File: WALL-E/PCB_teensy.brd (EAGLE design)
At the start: 92.8 x 115.8 mm, 44 parts, among them U4 R-78E5.0-0.5

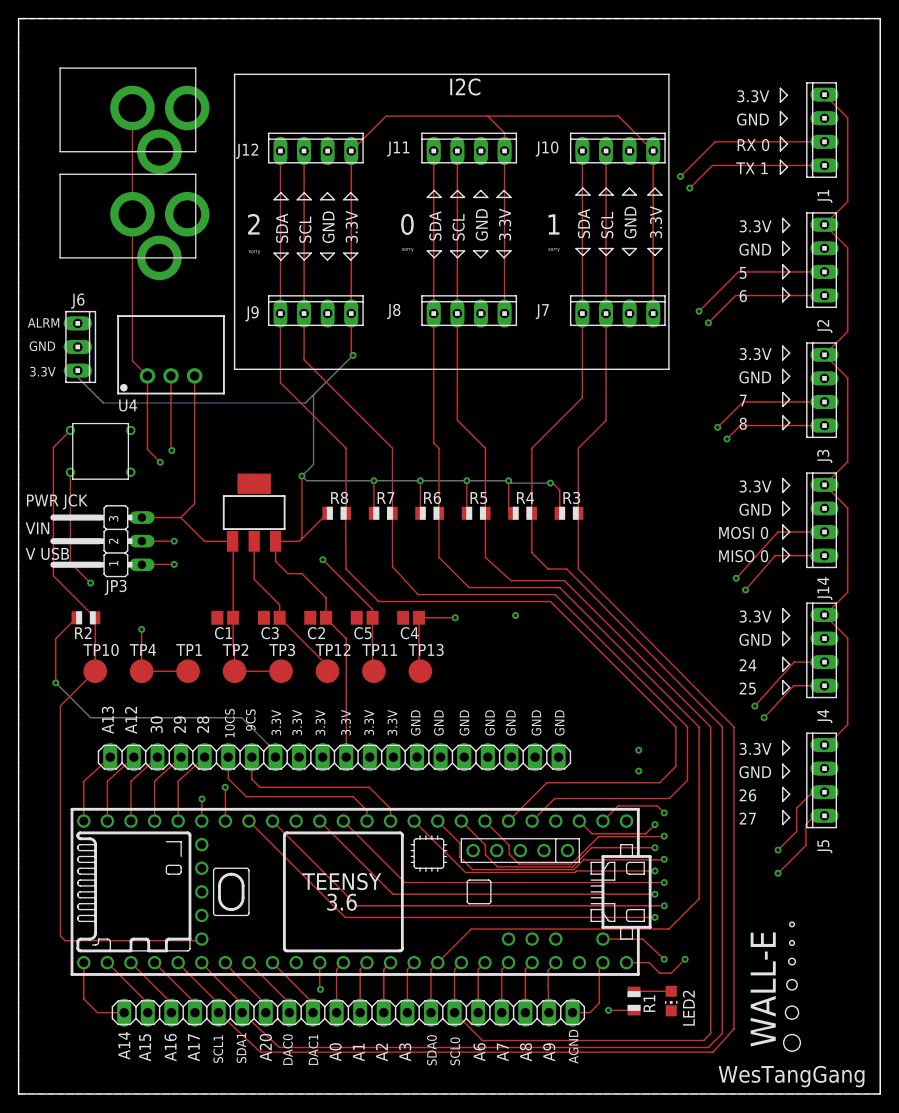
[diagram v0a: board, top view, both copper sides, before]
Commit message: removed extra top layer polygon and moved dimension to dimension layer. Also spaced out barrel jacks slightly
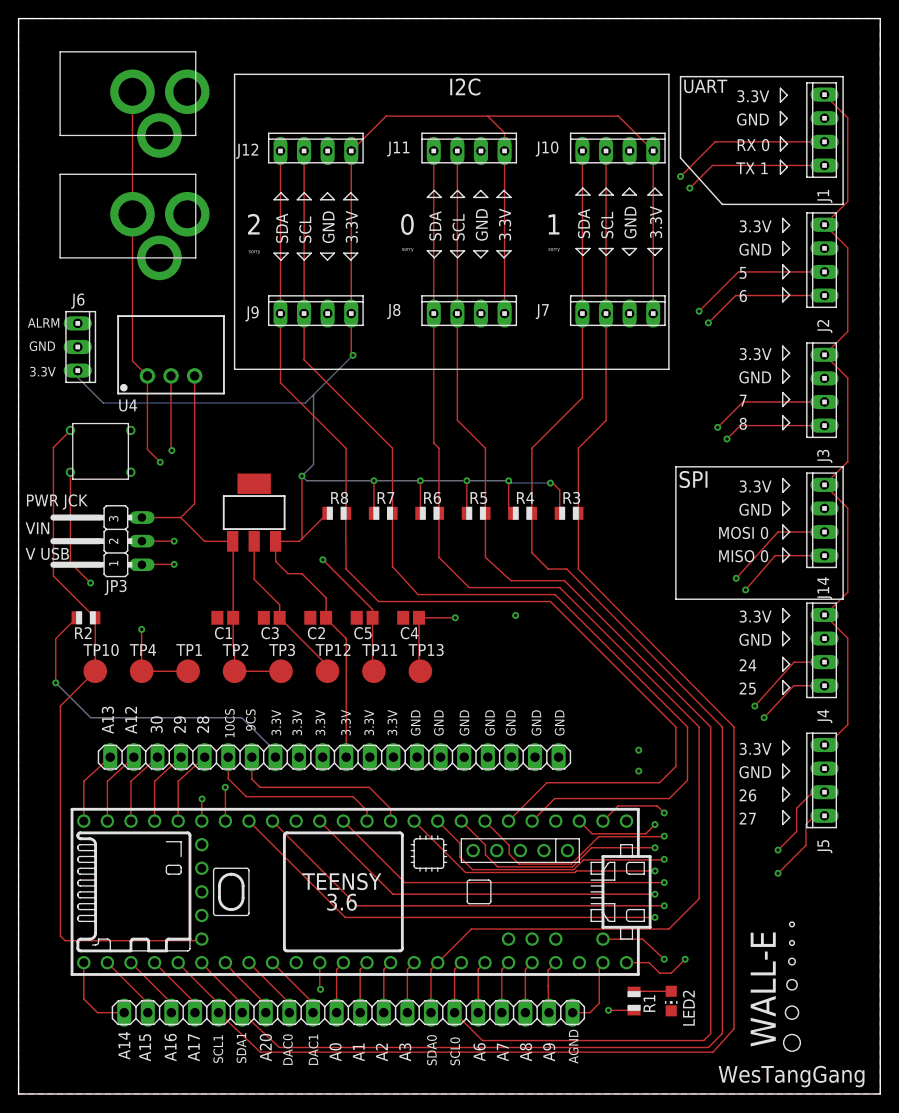
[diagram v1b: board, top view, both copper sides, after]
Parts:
- moved U$6 1.75 mm to (8.87, 107.8)
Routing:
- net +12V: track 67.7 -> 69.4 mm
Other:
- board text added: "SPI"
- board text added: "UART"

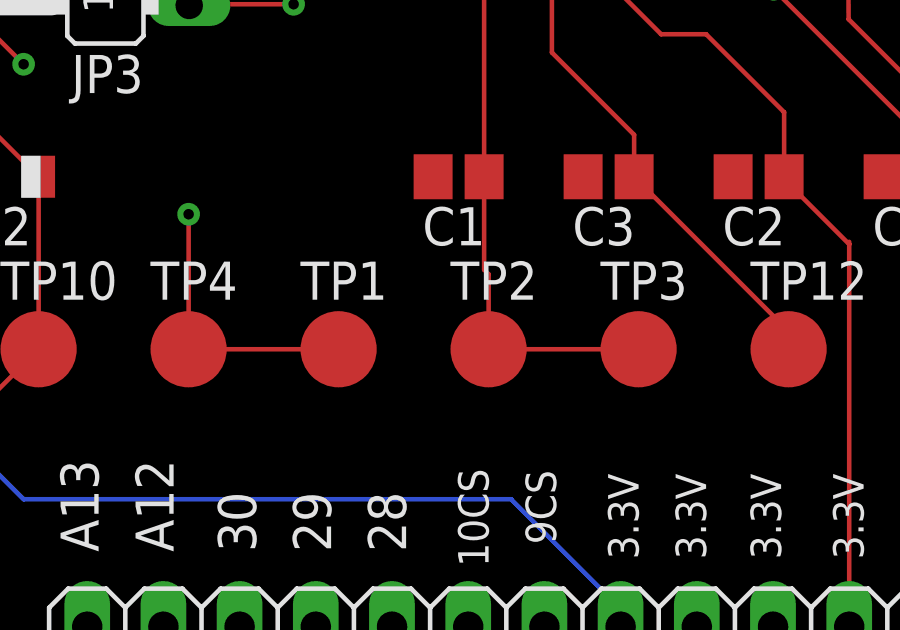
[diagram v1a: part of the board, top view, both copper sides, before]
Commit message: removed some test pins
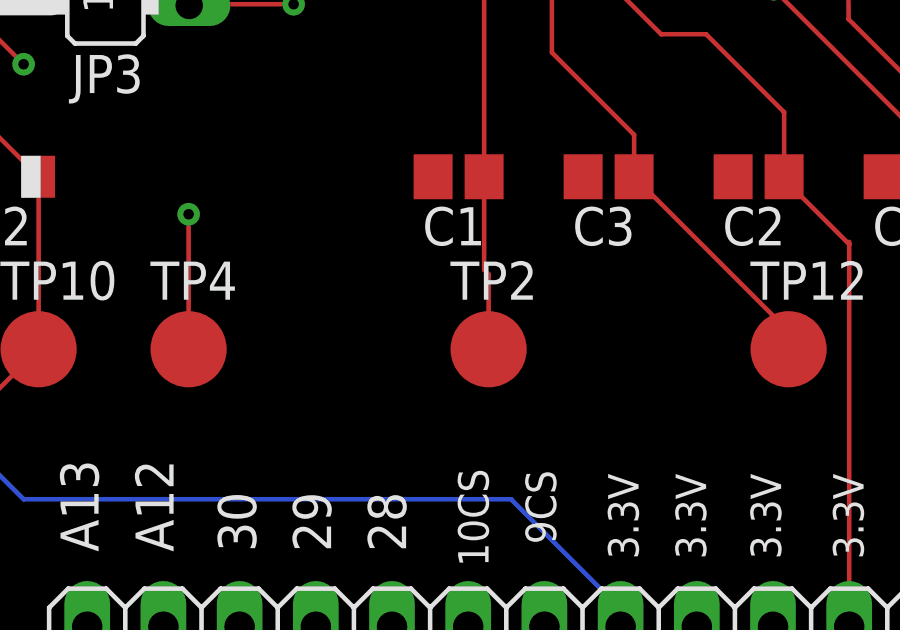
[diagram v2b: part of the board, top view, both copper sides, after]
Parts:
- removed TP1, TP3: PTR1B2,54, testpad:B2,54
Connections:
- net +12V: no longer TP1.TP
- net 5V: no longer TP3.TP
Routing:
- net 5V: track 45.9 -> 40.9 mm
- net +12V: track 69.4 -> 64.4 mm
- added copper zone on layer 15, net 3.3V
- removed copper zone on layer 2, net 3.3V

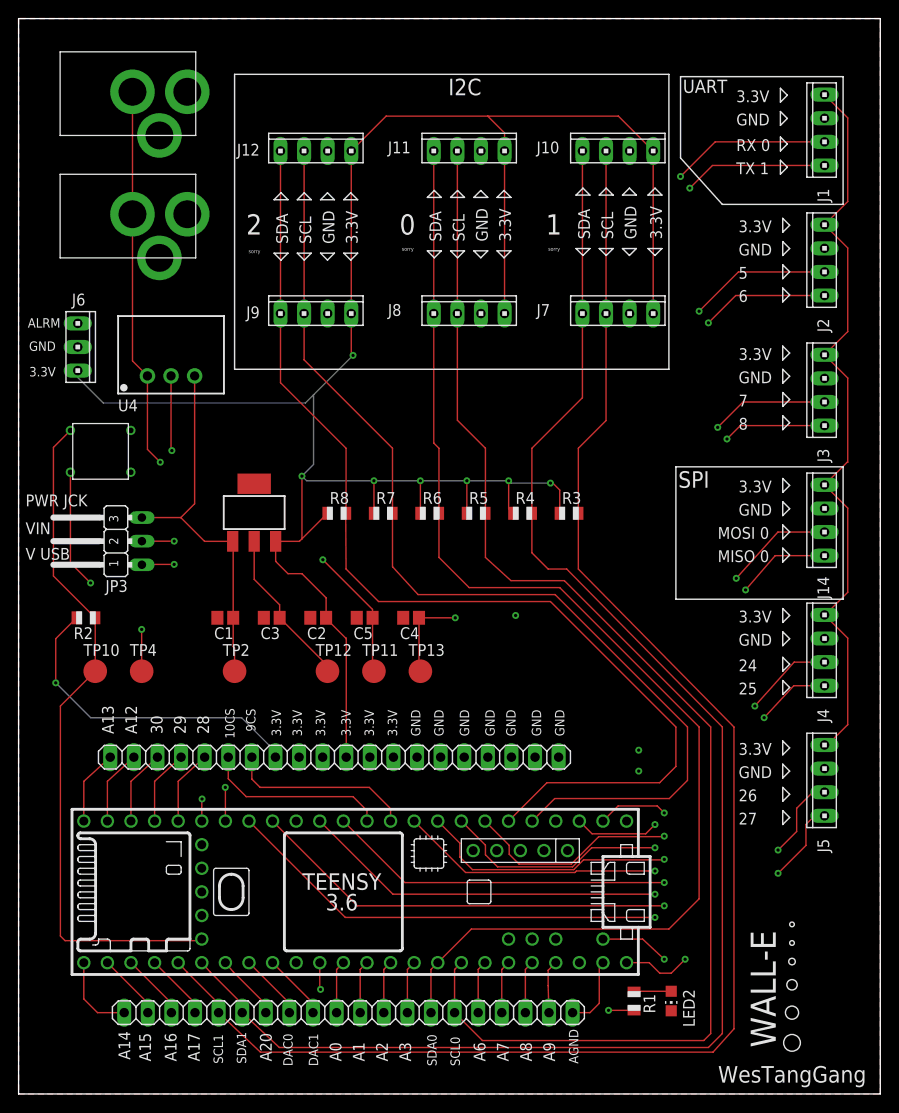
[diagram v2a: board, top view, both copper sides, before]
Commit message: removed 3.3v power routes, now components connect to the power plane
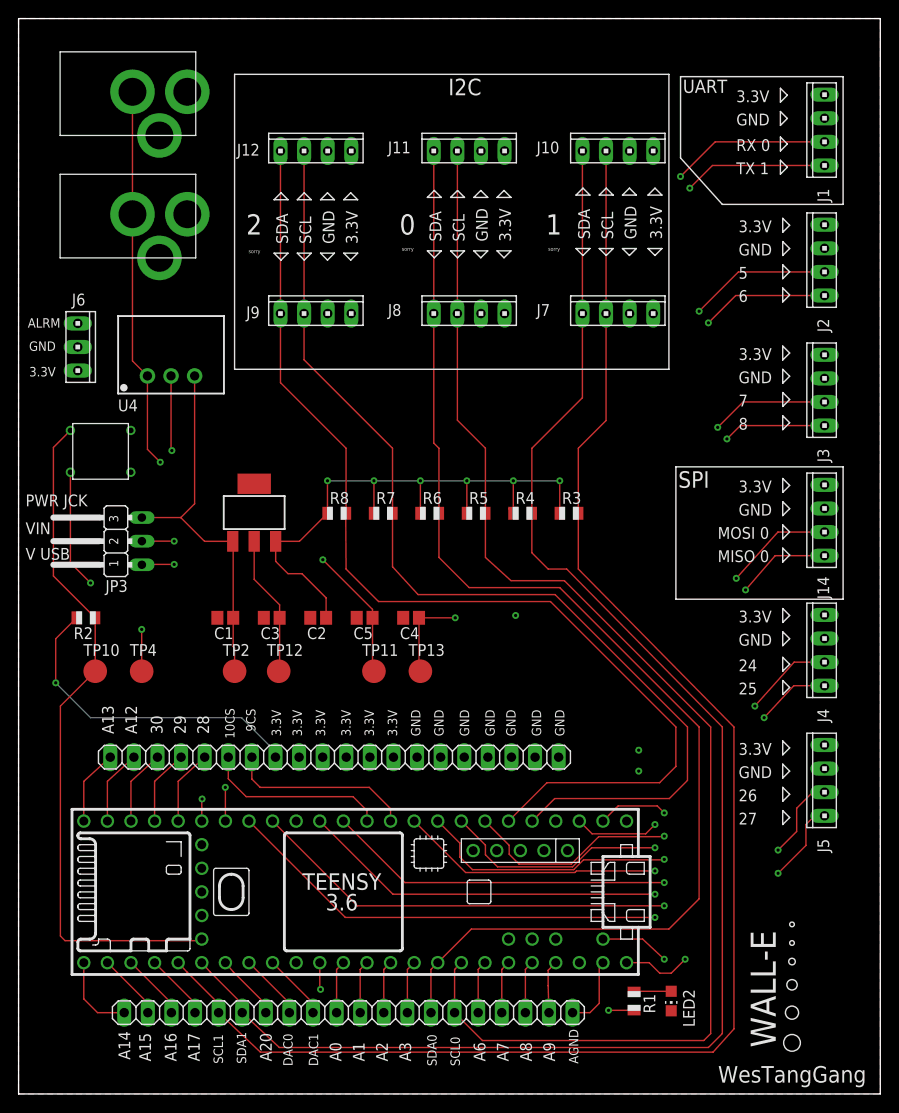
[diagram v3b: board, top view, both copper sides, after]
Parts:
- moved TP12 5.25 mm to (28.0, 45.5)
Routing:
- net 3.3V: track 342.3 -> 100.1 mm, vias 8 -> 7
- net ALARMPIN: track 95.5 -> 97.8 mm
- net N$3: track 17.2 -> 15.2 mm
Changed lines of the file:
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@@
 <attribute name="TP_SIGNAL_NAME" value="" x="38.25" y="45.5" size="1.778" layer="27" display="off"/>
 </element>
-<element name="TP12" library="testpad" library_urn="urn:adsk.eagle:library:385" package="B2,54" package3d_urn="urn:adsk.eagle:package:27948/1" value="PTR1B2,54" x="33.25" y="45.5">
-<attribute name="TP_SIGNAL_NAME" value="" x="33.25" y="45.5" size="1.778" layer="27" display="off"/>
+<element name="TP12" library="testpad" library_urn="urn:adsk.eagle:library:385" package="B2,54" package3d_urn="urn:adsk.eagle:package:27948/1" value="PTR1B2,54" x="28" y="45.5">
+<attribute name="TP_SIGNAL_NAME" value="" x="28" y="45.5" size="1.778" layer="27" display="off"/>
 </element>
 <element name="TP13" library="testpad" library_urn="urn:adsk.eagle:library:385" package="B2,54" package3d_urn="urn:adsk.eagle:package:27948/1" value="PTR1B2,54" x="43.25" y="45.5">
@@
 <wire x1="25.36" y1="55.39" x2="25.36" y2="59.4812" width="0.1524" layer="1"/>
 <wire x1="28.1" y1="52.65" x2="25.36" y2="55.39" width="0.1524" layer="1"/>
-<wire x1="28.1" y1="51.25" x2="33.25" y2="46.1" width="0.1524" layer="1"/>
-<wire x1="33.25" y1="46.1" x2="33.25" y2="45.5" width="0.1524" layer="1"/>
+<wire x1="28.1" y1="51.25" x2="28.1" y2="45.6" width="0.1524" layer="1"/>
+<wire x1="28.1" y1="45.6" x2="28" y2="45.5" width="0.1524" layer="1"/>
 </signal>
 <signal name="N$4">
@@
 <vertex x="0" y="115.75"/>
 </polygon>
-<wire x1="33.25" y1="62.5" x2="30.5" y2="59.75" width="0.1524" layer="1"/>
+<wire x1="33.25" y1="62.5" x2="30.2312" y2="59.4812" width="0.1524" layer="1"/>
 <wire x1="30.2312" y1="59.4812" x2="27.6714" y2="59.4812" width="0.1524" layer="1"/>
-<wire x1="35.81" y1="84" x2="35.81" y2="79.69" width="0.1524" layer="1"/>
-<wire x1="35.81" y1="79.69" x2="36" y2="79.5" width="0.1524" layer="1"/>
-<via x="36" y="79.5" extent="1-16" drill="0.35"/>
-<wire x1="36" y1="79.5" x2="31.75" y2="75.25" width="0.1524" layer="16"/>
-<via x="30.5" y="66.5" extent="1-16" drill="0.35"/>
-<wire x1="31.75" y1="75.25" x2="30.875" y2="74.375" width="0.1524" layer="16"/>
-<wire x1="30.5" y1="66.5" x2="30.5" y2="59.75" width="0.1524" layer="1"/>
-<wire x1="30.5" y1="59.75" x2="30.2312" y2="59.4812" width="0.1524" layer="1"/>
-<wire x1="6.37" y1="77.13" x2="6.37" y2="77.86" width="0.1524" layer="16"/>
-<wire x1="35.27" y1="49.08" x2="35.27" y2="49" width="0.1524" layer="1"/>
-<wire x1="35.27" y1="49" x2="35.27" y2="36.25" width="0.1524" layer="1"/>
-<wire x1="30.875" y1="74.375" x2="9.125" y2="74.375" width="0.1524" layer="16"/>
-<wire x1="9.125" y1="74.375" x2="6.37" y2="77.13" width="0.1524" layer="16"/>
-<wire x1="31.75" y1="75.25" x2="31.75" y2="67.75" width="0.1524" layer="16"/>
-<wire x1="31.75" y1="67.75" x2="30.5" y2="66.5" width="0.1524" layer="16"/>
+<via x="33.25" y="66" extent="1-16" drill="0.35"/>
 <wire x1="29" y1="56" x2="30.5" y2="56" width="0.1524" layer="1"/>
 <wire x1="29" y1="56" x2="27.6714" y2="57.3286" width="0.1524" layer="1"/>
 <wire x1="27.6714" y1="57.3286" x2="27.6714" y2="59.4812" width="0.1524" layer="1"/>
-<wire x1="35.81" y1="101.5" x2="35.81" y2="84" width="0.1524" layer="1"/>
-<wire x1="35.81" y1="101.5" x2="39.56" y2="105.25" width="0.1524" layer="1"/>
-<wire x1="39.56" y1="105.25" x2="50.5" y2="105.25" width="0.1524" layer="1"/>
-<wire x1="50.5" y1="105.25" x2="52.31" y2="103.44" width="0.1524" layer="1"/>
-<wire x1="52.31" y1="103.44" x2="52.31" y2="101.5" width="0.1524" layer="1"/>
-<wire x1="68.31" y1="101.5" x2="64.56" y2="105.25" width="0.1524" layer="1"/>
-<wire x1="64.56" y1="105.25" x2="50.5" y2="105.25" width="0.1524" layer="1"/>
-<wire x1="52.31" y1="101.5" x2="52.31" y2="84" width="0.1524" layer="1"/>
-<wire x1="86.75" y1="107.56" x2="89.25" y2="105.06" width="0.1524" layer="1"/>
-<wire x1="89.25" y1="96.06" x2="86.75" y2="93.56" width="0.1524" layer="1"/>
-<wire x1="89.25" y1="105.06" x2="89.25" y2="96.06" width="0.1524" layer="1"/>
-<wire x1="86.75" y1="93.56" x2="89.25" y2="91.06" width="0.1524" layer="1"/>
-<wire x1="89.25" y1="82.06" x2="86.75" y2="79.56" width="0.1524" layer="1"/>
-<wire x1="89.25" y1="91.06" x2="89.25" y2="82.06" width="0.1524" layer="1"/>
-<wire x1="86.75" y1="79.56" x2="89.25" y2="77.06" width="0.1524" layer="1"/>
-<wire x1="89.25" y1="77.06" x2="89.25" y2="68" width="0.1524" layer="1"/>
-<wire x1="89.25" y1="68" x2="89.19" y2="68" width="0.1524" layer="1"/>
-<wire x1="89.19" y1="68" x2="86.75" y2="65.56" width="0.1524" layer="1"/>
-<wire x1="86.75" y1="65.56" x2="89.25" y2="63.06" width="0.1524" layer="1"/>
-<wire x1="89.25" y1="63.06" x2="89.25" y2="54" width="0.1524" layer="1"/>
-<wire x1="89.25" y1="54" x2="86.81" y2="51.56" width="0.1524" layer="1"/>
-<wire x1="86.81" y1="51.56" x2="86.75" y2="51.56" width="0.1524" layer="1"/>
-<wire x1="86.75" y1="51.56" x2="89.25" y2="49.06" width="0.1524" layer="1"/>
-<wire x1="89.25" y1="49.06" x2="89.25" y2="39.75" width="0.1524" layer="1"/>
-<wire x1="89.25" y1="39.75" x2="87.06" y2="37.56" width="0.1524" layer="1"/>
-<wire x1="87.06" y1="37.56" x2="86.75" y2="37.56" width="0.1524" layer="1"/>
-<wire x1="68.31" y1="84" x2="68.31" y2="101.5" width="0.1524" layer="1"/>
-<wire x1="35.27" y1="49" x2="33.1" y2="51.17" width="0.1524" layer="1"/>
-<wire x1="33.1" y1="51.17" x2="33.1" y2="51.25" width="0.1524" layer="1"/>
 <wire x1="30.5" y1="56" x2="33.1" y2="53.4" width="0.1524" layer="1"/>
 <wire x1="33.1" y1="53.4" x2="33.1" y2="51.25" width="0.1524" layer="1"/>
-<wire x1="58.25" y1="62.5" x2="58.25" y2="65" width="0.1524" layer="1"/>
-<wire x1="58.25" y1="65" x2="57.25" y2="66" width="0.1524" layer="1"/>
-<wire x1="57.25" y1="66" x2="57.25" y2="65.75" width="0.1524" layer="1"/>
-<via x="57.25" y="65.75" extent="1-16" drill="0.35"/>
-<wire x1="57.25" y1="65.75" x2="53" y2="65.75" width="0.1524" layer="16"/>
-<wire x1="53" y1="65.75" x2="52.75" y2="66" width="0.1524" layer="16"/>
-<via x="52.75" y="66" extent="1-16" drill="0.35"/>
-<wire x1="52.75" y1="66" x2="52.75" y2="63" width="0.1524" layer="1"/>
+<via x="58.25" y="66" extent="1-16" drill="0.35"/>
+<via x="53.25" y="66" extent="1-16" drill="0.35"/>
 <wire x1="52.75" y1="63" x2="53.25" y2="62.5" width="0.1524" layer="1"/>
-<wire x1="52.75" y1="66" x2="48.25" y2="66" width="0.1524" layer="16"/>
+<wire x1="53.25" y1="66" x2="48.25" y2="66" width="0.1524" layer="16"/>
 <via x="48.25" y="66" extent="1-16" drill="0.35"/>
 <wire x1="48.25" y1="66" x2="48.25" y2="62.5" width="0.1524" layer="1"/>
@@
 <via x="38.25" y="66" extent="1-16" drill="0.35"/>
 <wire x1="38.25" y1="66" x2="38.25" y2="62.5" width="0.1524" layer="1"/>
-<wire x1="38.25" y1="66" x2="31" y2="66" width="0.1524" layer="16"/>
-<wire x1="31" y1="66" x2="30.5" y2="66.5" width="0.1524" layer="16"/>
 <wire x1="6.25" y1="51.25" x2="4" y2="49" width="0.1524" layer="1"/>
 <wire x1="4" y1="49" x2="4" y2="44.25" width="0.1524" layer="1"/>
@@
 <wire x1="24" y1="40.5" x2="27.65" y2="36.85" width="0.1524" layer="16"/>
 <wire x1="27.65" y1="36.85" x2="27.65" y2="36.25" width="0.1524" layer="16"/>
+<wire x1="33.25" y1="62.5" x2="33.25" y2="66" width="0.1524" layer="1"/>
+<wire x1="33.25" y1="66" x2="38.25" y2="66" width="0.1524" layer="16"/>
+<wire x1="53.25" y1="66" x2="58.25" y2="66" width="0.1524" layer="16"/>
+<wire x1="53.25" y1="66" x2="53.25" y2="62.5" width="0.1524" layer="1"/>
+<wire x1="58.25" y1="66" x2="58.25" y2="62.5" width="0.1524" layer="1"/>
 </signal>
 <signal name="0/RX">
@@
 <contactref element="U$1" pad="2"/>
 <via x="53.5" y="51.5" extent="1-16" drill="0.35"/>
-<wire x1="57.82" y1="29.37" x2="57.82" y2="35.159075" width="0.1524" layer="2"/>
-<wire x1="57.82" y1="35.159075" x2="57.1394" y2="35.839675" width="0.1524" layer="2"/>
-<wire x1="57.1394" y1="47.8606" x2="53.5" y2="51.5" width="0.1524" layer="2"/>
-<wire x1="57.1394" y1="35.839675" x2="57.1394" y2="47.8606" width="0.1524" layer="2"/>
 <wire x1="53.5" y1="51.5" x2="46.75" y2="58.25" width="0.1524" layer="15"/>
 <wire x1="46.75" y1="58.25" x2="46.75" y2="66.5" width="0.1524" layer="15"/>
@@
 <wire x1="9.43" y1="86" x2="6.37" y2="82.94" width="0.1524" layer="15"/>
 <wire x1="22.5" y1="86" x2="9.43" y2="86" width="0.1524" layer="15"/>
+<wire x1="53.5" y1="51.5" x2="60.5" y2="44.5" width="0.1524" layer="2"/>
+<wire x1="60.5" y1="32.05" x2="57.82" y2="29.37" width="0.1524" layer="2"/>
+<wire x1="60.5" y1="44.5" x2="60.5" y2="32.05" width="0.1524" layer="2"/>
 </signal>
 <signal name="5">
